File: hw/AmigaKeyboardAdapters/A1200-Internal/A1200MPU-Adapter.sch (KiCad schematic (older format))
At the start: 8 parts, among them P1 Conn_02x03_Odd_Even, U1 A1200U13_REV_PLCC44

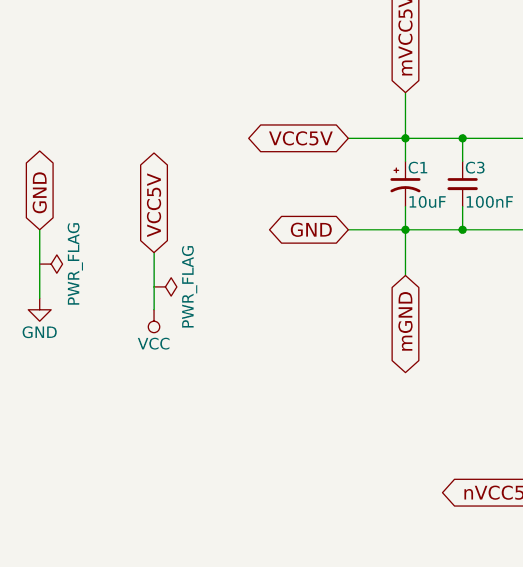
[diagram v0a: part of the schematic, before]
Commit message: Updated PWR_FLAGs
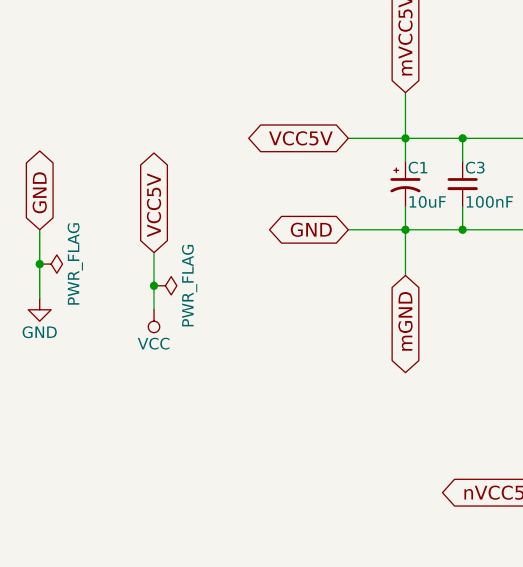
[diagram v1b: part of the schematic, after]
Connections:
- wire segments 26 -> 28
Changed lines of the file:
@@
 GND
 Wire Wire Line
-	2500 1600 2500 1900
+	2500 1600 2500 1750
 $Comp
 L power:PWR_FLAG #FLG02
@@
 VCC5V
 Wire Wire Line
-	3000 1700 3000 1950
+	3000 1700 3000 1845
 $Comp
 L power:VCC #PWR03
@@
 L power:PWR_FLAG #FLG04
 U 1 1 5BE8A5B2
-P 3000 1850
-F 0 "#FLG04" H 3000 1925 50  0001 C CNN
-F 1 "PWR_FLAG" H 3000 2000 50  0000 C CNN
-F 2 "" H 3000 1850 50  0001 C CNN
-F 3 "" H 3000 1850 50  0001 C CNN
-	1    3000 1850
+P 3000 1845
+F 0 "#FLG04" H 3000 1920 50  0001 C CNN
+F 1 "PWR_FLAG" H 3000 1995 50  0000 C CNN
+F 2 "" H 3000 1845 50  0001 C CNN
+F 3 "" H 3000 1845 50  0001 C CNN
+	1    3000 1845
 	0    1    1    0
 $EndComp
@@
 	1    0    0    -1
 $EndComp
+Connection ~ 3000 1845
+Wire Wire Line
+	3000 1845 3000 1950
+Connection ~ 2500 1750
+Wire Wire Line
+	2500 1750 2500 1900
 $EndSCHEMATC

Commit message: RetroBitLab library
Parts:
- U1: symbol AmigaComponents:A1200U13_REV_PLCC44 -> RetroBitLab:A1200U13_REV_PLCC44
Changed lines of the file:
@@
 $EndDescr
 $Comp
-L AmigaComponents:A1200U13_REV_PLCC44 U1
+L RetroBitLab:A1200U13_REV_PLCC44 U1
 U 1 1 5BE895D2
 P 5750 3650

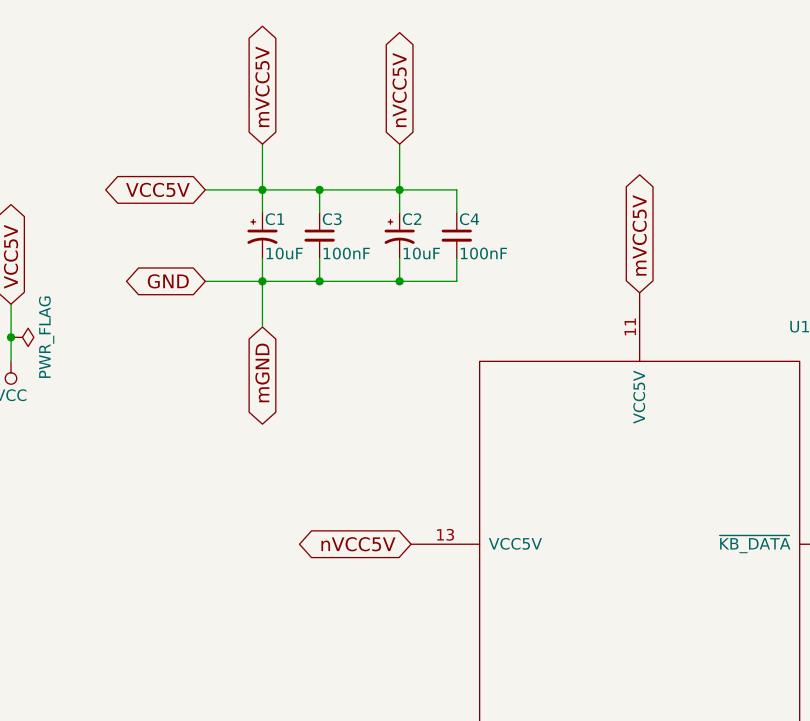
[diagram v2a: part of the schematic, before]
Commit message: Updated from Library. /IRQ is not tied at VCC anymore.
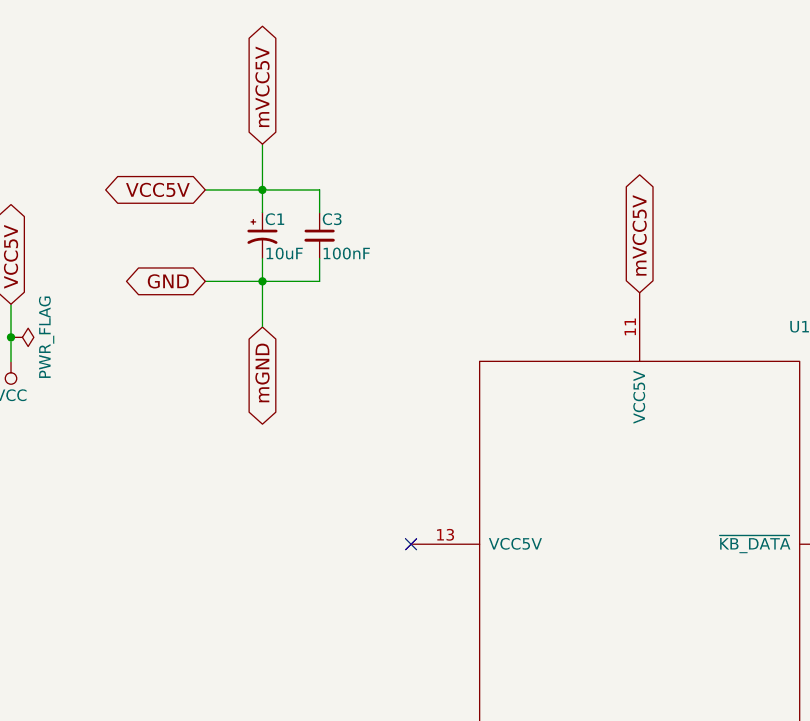
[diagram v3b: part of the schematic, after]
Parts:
- removed C2: 10uF, Capacitor_Tantalum_SMD:CP_EIA-3216-12_Kemet-S_Pad1.58x1.35mm_HandSolder, symbol Device:CP1_Small
- removed C4: 100nF, Capacitor_SMD:C_1206_3216Metric_Pad1.33x1.80mm_HandSolder, symbol Device:C_Small
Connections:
- net labels removed: nVCC5V
- wire segments 28 -> 19
- no-connect marks 0 -> 1
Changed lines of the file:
@@
 	1    0    0    -1
 $EndComp
-Text GLabel 4750 2750 0    60   BiDi ~ 0
-nVCC5V
 Text GLabel 5750 1650 1    60   BiDi ~ 0
 mVCC5V
@@
 Wire Wire Line
 	3850 1200 4100 1200
-Wire Wire Line
-	4700 1000 4700 1200
 Connection ~ 4100 1200
 Wire Wire Line
@@
 Text GLabel 4100 1000 1    60   BiDi ~ 0
 mVCC5V
-Text GLabel 4700 1000 1    60   BiDi ~ 0
-nVCC5V
-Connection ~ 4700 1200
 Text GLabel 5750 5650 3    60   BiDi ~ 0
 mGND
@@
 $EndComp
 Wire Wire Line
-	4950 1200 4950 1300
-Wire Wire Line
-	4950 1600 4950 1500
-Connection ~ 4700 1600
-Wire Wire Line
 	4350 1300 4350 1200
-Connection ~ 4350 1200
 Wire Wire Line
 	4350 1500 4350 1600
-Connection ~ 4350 1600
 Wire Wire Line
 	4100 1200 4100 1300
@@
 	4100 1200 4350 1200
 Wire Wire Line
-	4700 1200 4700 1300
-Wire Wire Line
-	4700 1200 4950 1200
-Wire Wire Line
 	4100 1600 4100 1800
 Wire Wire Line
 	4100 1600 4350 1600
-Wire Wire Line
-	4700 1600 4950 1600
-Wire Wire Line
-	4350 1200 4700 1200
-Wire Wire Line
-	4350 1600 4700 1600
 $Comp
 L Connector_Generic:Conn_02x03_Odd_Even P1
@@
 	0    -1   -1   0
 $EndComp
-Wire Wire Line
-	4700 1500 4700 1600
-$Comp
-L Device:CP1_Small C2
-U 1 1 636E678B
-P 4700 1400
-F 0 "C2" H 4710 1470 50  0000 L CNN
-F 1 "10uF" H 4710 1320 50  0000 L CNN
-F 2 "Capacitor_Tantalum_SMD:CP_EIA-3216-12_Kemet-S_Pad1.58x1.35mm_HandSolder" H 4700 1400 50  0001 C CNN
-F 3 "https://datasheet.lcsc.com/lcsc/1811151641_Sunlord-TC212A106K016Y_C108529.pdf" H 4700 1400 50  0001 C CNN
-F 4 "C108529" H 4700 1400 50  0001 C CNN "LCSC"
-	1    4700 1400
-	1    0    0    -1
-$EndComp
-$Comp
-L Device:C_Small C4
-U 1 1 636E7056
-P 4950 1400
-F 0 "C4" H 4960 1470 50  0000 L CNN
-F 1 "100nF" H 4960 1320 50  0000 L CNN
-F 2 "Capacitor_SMD:C_1206_3216Metric_Pad1.33x1.80mm_HandSolder" H 4950 1400 50  0001 C CNN
-F 3 "https://datasheet.lcsc.com/lcsc/1810221109_Samsung-Electro-Mechanics-CL31B104KBCNNNC_C24497.pdf" H 4950 1400 50  0001 C CNN
-F 4 "C24497" H 4950 1400 50  0001 C CNN "LCSC"
-	1    4950 1400
-	1    0    0    -1
-$EndComp
 Connection ~ 3000 1845
 Wire Wire Line
@@
 Wire Wire Line
 	2500 1750 2500 1900
+NoConn ~ 4750 2750
 $EndSCHEMATC
